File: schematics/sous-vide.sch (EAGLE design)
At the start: 33 parts, among them IC1 MEGA32-P

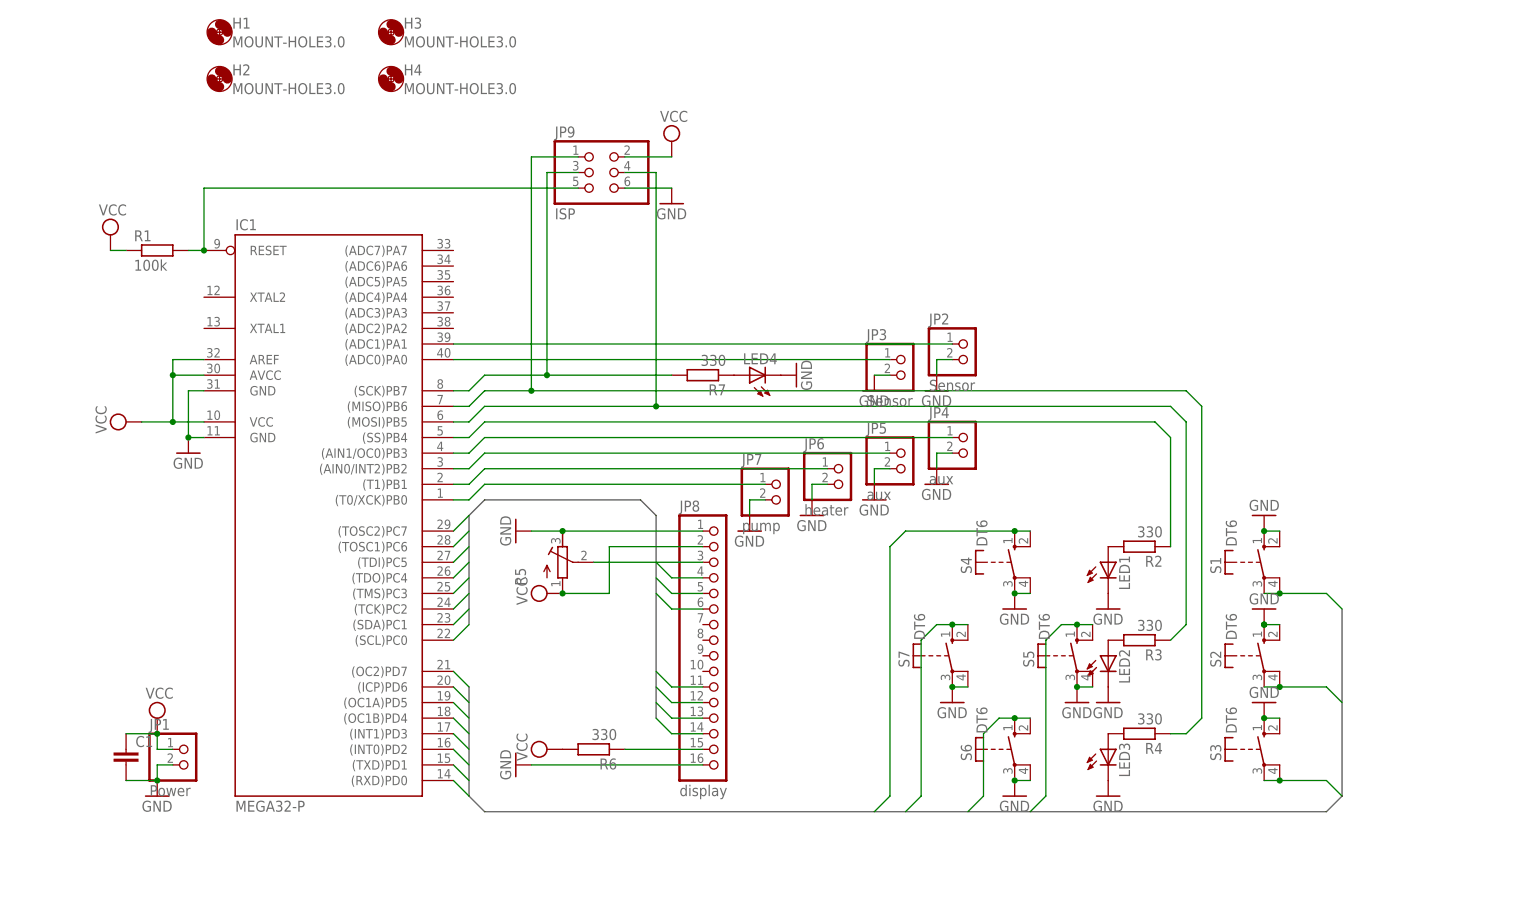
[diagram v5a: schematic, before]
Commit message: Switched to ATmega328 and updated schematics and board.
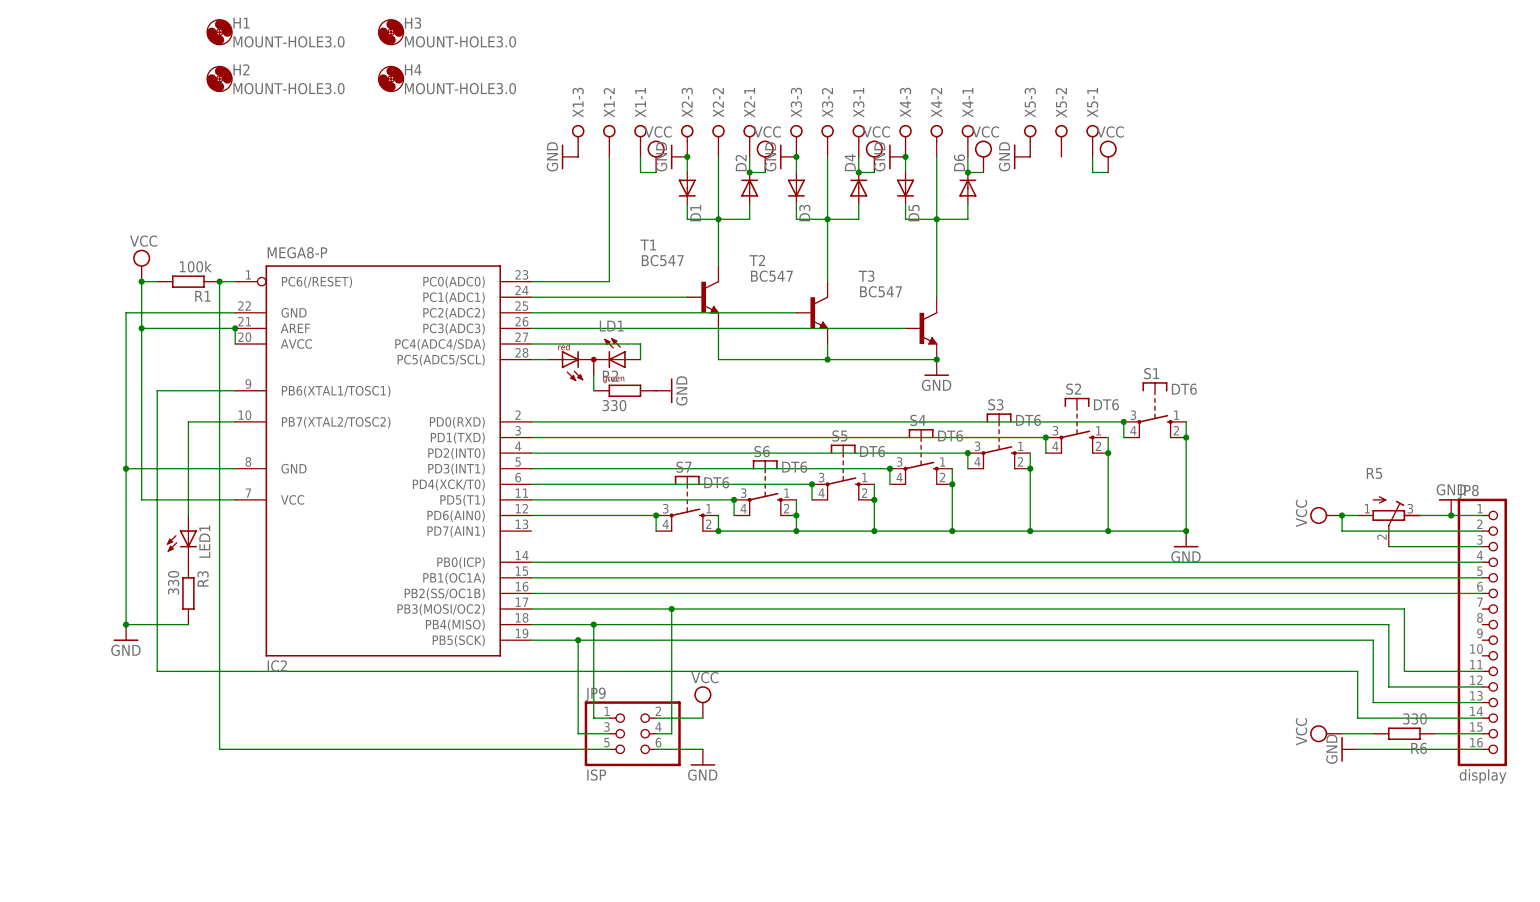
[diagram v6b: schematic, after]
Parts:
- removed C1: (no value), resistor:C-EU025-025X050
- removed IC1: MEGA32-P, atmel:MEGA32-P
- removed JP1: Power, pinhead:PINHD-1X2
- removed JP2, JP3: Sensor, pinhead:PINHD-1X2
- removed JP4, JP5: aux, pinhead:PINHD-1X2
- removed JP6: heater, pinhead:PINHD-1X2
- removed JP7: pump, pinhead:PINHD-1X2
- removed LED2, LED3, LED4: (no value), led:LED3MM
- removed R4, R7: 330, rcl:R-EU_0207/2V
- added D1, D2, D3, D4, D5, D6: (no value), diode:DIODE-D-2.5
- added IC2: MEGA8-P, atmel:MEGA8-P
- added LD1: (no value), led:DUOLED-RG-C
- added T1, T2, T3: BC547, transistor:BC547
- added X1, X2, X3, X4, X5: (no value), con-wago-508:W237-03P
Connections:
- removed net BUTTON0: IC1.(RXD)PD0, S1.P, S1.P@1
- removed net BUTTON1: IC1.(TXD)PD1, S2.P, S2.P@1
- removed net BUTTON2: IC1.(INT0)PD2, S3.P, S3.P@1
- removed net BUTTON3: IC1.(INT1)PD3, S4.S, S4.S@1
- removed net BUTTON4: IC1.(OC1B)PD4, S5.S, S5.S@1
- removed net BUTTON5: IC1.(OC1A)PD5, S6.S, S6.S@1
- removed net BUTTON6: IC1.(ICP)PD6, S7.S, S7.S@1
- removed net BUTTON7: IC1.(OC2)PD7
- removed net DISPLAY0: IC1.(SCL)PC0
- removed net DISPLAY1: IC1.(SDA)PC1, JP8.4
- removed net DISPLAY2: IC1.(TCK)PC2, JP8.5
- removed net DISPLAY3: IC1.(TMS)PC3, JP8.6
- removed net DISPLAY4: IC1.(TDO)PC4, JP8.11
- removed net DISPLAY5: IC1.(TDI)PC5, JP8.12
- removed net DISPLAY6: IC1.(TOSC1)PC6, JP8.13
- removed net DISPLAY7: IC1.(TOSC2)PC7, JP8.14
- removed net N$10: IC1.(SS)PB4, R2.1
- removed net N$11: IC1.(MOSI)PB5, JP9.4, R3.1
- removed net N$12: IC1.(ADC0)PA0, JP3.1
- removed net N$13: IC1.(MISO)PB6, JP9.1, R4.1
- removed net N$16: LED4.A, R7.1
- removed net N$17: IC1.(SCK)PB7, JP9.3, R7.2
- new net N$18: IC2.PB5(SCK), JP8.13, JP9.3
- new net N$19: IC2.PB4(MISO), JP8.12, JP9.1
- new net N$20: IC2.PB0(ICP), JP8.4
- new net N$21: IC2.PB1(OC1A), JP8.5
- new net N$22: IC2.PB2(SS/OC1B), JP8.6
- new net N$23: IC2.PB6(XTAL1/TOSC1), JP8.14
- new net N$24: IC2.PB3(MOSI/OC2), JP8.11, JP9.4
- new net N$26: IC2.PD6(AIN0), S7.P, S7.P@1
- new net N$28: IC2.PD5(T1), S6.P, S6.P@1
- new net N$29: D5.C, D6.A, T3.C, X4-2.KL
- new net N$30: IC2.PD3(INT1), S4.P, S4.P@1
- new net N$31: IC2.PC6(/RESET), JP9.5, R1.1
- new net N$32: IC2.PD4(XCK/T0), S5.P, S5.P@1
- new net N$33: D3.C, D4.A, T2.C, X3-2.KL
- new net N$34: D1.C, D2.A, T1.C, X2-2.KL
- new net N$35: IC2.PD2(INT0), S3.P, S3.P@1
- new net N$36: IC2.PD0(RXD), S1.P, S1.P@1
- new net N$37: IC2.PD1(TXD), S2.P, S2.P@1
- net GND: now also D1.A, D3.A, D5.A, IC2.GND, IC2.GND@1, R2.2, R3.2, S4.S, S4.S@1, S5.S, S5.S@1, S6.S, S6.S@1, S7.S, S7.S@1, T1.E, T2.E, T3.E, X1-3.KL, X2-3.KL, X3-3.KL, X4-3.KL, X5-3.KL; no longer C1.2, IC1.GND, IC1.GND@1, JP1.2, JP2.2, JP3.2, JP4.2, JP5.2, JP6.2, JP7.2, LED1.C, LED2.C, LED3.C, LED4.C, S4.P, S4.P@1, S5.P, S5.P@1, S6.P, S6.P@1, S7.P, S7.P@1
- net N$1: now also LED1.C, R3.1; no longer IC1.(T0/XCK)PB0, JP7.1
- net N$2: now also IC2.PB7(XTAL2/TOSC2), LED1.A; no longer IC1.(T1)PB1, JP6.1
- net N$3: now also IC2.PC0(ADC0), X1-2.KL; no longer IC1.RESET, JP9.5, R1.2
- net N$4: now also IC2.PC1(ADC1), T1.B; no longer IC1.(AIN0/INT2)PB2, JP5.1
- net N$5: now also IC2.PC2(ADC2), T2.B; no longer IC1.(AIN1/OC0)PB3, JP4.1
- net N$6: now also IC2.PC3(ADC3), T3.B; no longer IC1.(ADC1)PA1, JP2.1
- net N$7: now also LD1.C, R2.1; no longer LED3.A, R4.2
- net N$8: now also IC2.PC5(ADC5/SCL), LD1.AR; no longer LED2.A, R3.2
- net N$9: now also IC2.PC4(ADC4/SDA), LD1.AG; no longer LED1.A, R2.2
- net VCC: now also D2.C, D4.C, D6.C, IC2.AREF, IC2.AVCC, IC2.VCC@1, R1.2, X1-1.KL, X2-1.KL, X3-1.KL, X4-1.KL, X5-1.KL; no longer C1.1, IC1.AREF, IC1.AVCC, IC1.VCC, JP1.1, R1.1
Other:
- moved on the sheet: JP8, JP9, LED1, R1, R2, R3, R5, R6, S1, S2, S3, S4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

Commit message: Changed connectors and renumbered parts on schematic and board.
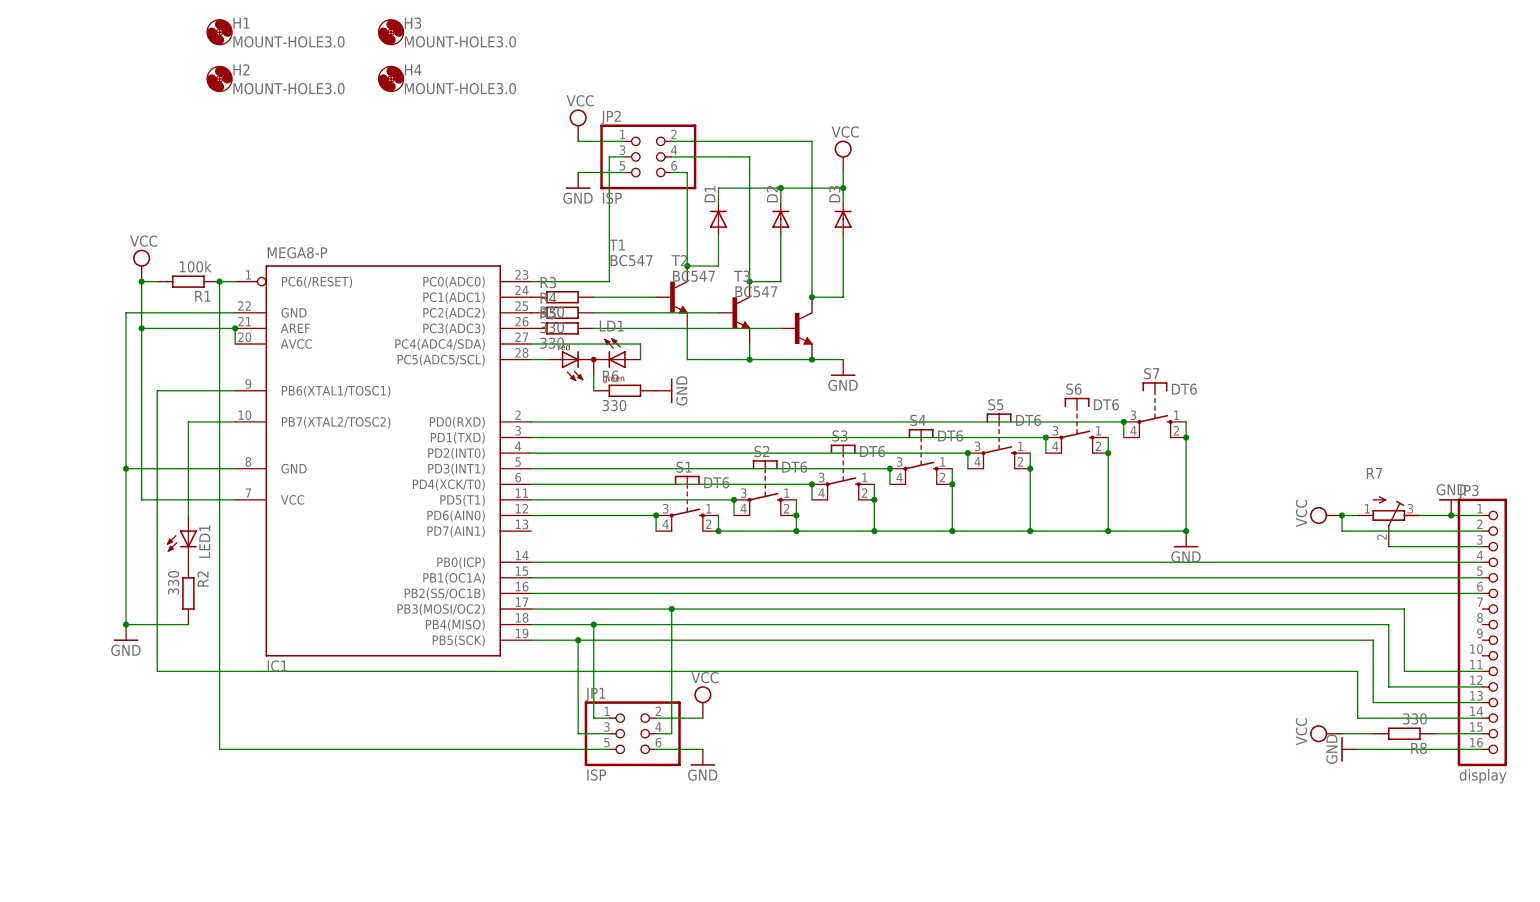
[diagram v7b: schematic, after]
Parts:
- removed D4, D5, D6: (no value), diode:DIODE-D-2.5
- removed X1, X2, X3, X4, X5: (no value), con-wago-508:W237-03P
- added JP2: ISP, pinhead:PINHD-2X3
- added R4, R8: 330, rcl:R-EU_0207/2V
- added R7: (no value), resistor:R-TRIMM3339P
- R5: value (none) -> 330; device resistor:R-TRIMM3339P -> rcl:R-EU_0207/2V
- renumbered IC2 to IC1, JP8 to JP3, JP9 to JP1
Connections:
- removed net N$29: D5.C, D6.A, T3.C, X4-2.KL
- removed net N$33: D3.C, D4.A, T2.C, X3-2.KL
- removed net N$34: D1.C, D2.A, T1.C, X2-2.KL
- new net N$10: R3.2, T1.B
- new net N$11: R4.2, T2.B
- new net N$12: R5.2, T3.B
- new net N$13: D1.A, JP2.6, T1.C
- new net N$16: D2.A, JP2.4, T2.C
- new net N$17: D3.A, JP2.2, T3.C
- net GND: now also JP2.5, R6.2, R7.A; no longer D1.A, D3.A, D5.A, R3.2, R5.A, X1-3.KL, X2-3.KL, X3-3.KL, X4-3.KL, X5-3.KL
- net N$1: now also R2.1; no longer R3.1
- net N$14: now also R7.S; no longer R5.S
- net N$15: now also R8.1; no longer R6.1
- net N$26: now also S1.P, S1.P@1; no longer S7.P, S7.P@1
- net N$28: now also S2.P, S2.P@1; no longer S6.P, S6.P@1
- net N$3: now also JP2.3; no longer X1-2.KL
- net N$32: now also S3.P, S3.P@1; no longer S5.P, S5.P@1
- net N$35: now also S5.P, S5.P@1; no longer S3.P, S3.P@1
- net N$36: now also S7.P, S7.P@1; no longer S1.P, S1.P@1
- net N$37: now also S6.P, S6.P@1; no longer S2.P, S2.P@1
- net N$4: now also R3.1; no longer T1.B
- net N$5: now also R4.1; no longer T2.B
- net N$6: now also R5.1; no longer T3.B
- net N$7: now also R6.1; no longer R2.1
- net VCC: now also D1.C, D3.C, JP2.1, R7.E, R8.2; no longer D4.C, D6.C, R5.E, R6.2, X1-1.KL, X2-1.KL, X3-1.KL, X4-1.KL, X5-1.KL
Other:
- moved on the sheet: D1, D2, D3, R2, R3, R6, S1, S2, S3, S5, S6, S7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

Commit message: minor tweaks in component placement, sent to pcb manufacturer
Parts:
- JP2: value ISP -> IO
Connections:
- net N$31: now also R1.2; no longer R1.1
- net VCC: now also R1.1; no longer R1.2
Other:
- moved on the sheet: R1
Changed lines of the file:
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@@
 <part name="R4" library="rcl" deviceset="R-EU_" device="0207/2V" value="330"/>
 <part name="R5" library="rcl" deviceset="R-EU_" device="0207/2V" value="330"/>
-<part name="JP2" library="pinhead" deviceset="PINHD-2X3" device="" value="ISP"/>
+<part name="JP2" library="pinhead" deviceset="PINHD-2X3" device="" value="IO"/>
 </parts>
 <sheets>
@@
 <instances>
 <instance part="SUPPLY1" gate="G$1" x="7.62" y="93.98"/>
-<instance part="R1" gate="G$1" x="15.24" y="91.44" rot="R180"/>
+<instance part="R1" gate="G$1" x="15.24" y="91.44"/>
 <instance part="JP3" gate="A" x="228.6" y="35.56"/>
 <instance part="S7" gate="1" x="172.72" y="68.58" rot="R270"/>
@@
 <junction x="22.86" y="83.82"/>
 <wire x1="22.86" y1="83.82" x2="7.62" y2="83.82" width="0.1524" layer="91"/>
-<pinref part="R1" gate="G$1" pin="2"/>
-<wire x1="10.16" y1="91.44" x2="7.62" y2="91.44" width="0.1524" layer="91"/>
+<junction x="7.62" y="83.82"/>
+<pinref part="R1" gate="G$1" pin="1"/>
+<wire x1="7.62" y1="91.44" x2="10.16" y2="91.44" width="0.1524" layer="91"/>
 <junction x="7.62" y="91.44"/>
-<junction x="7.62" y="83.82"/>
 </segment>
 <segment>
@@
 <pinref part="JP1" gate="A" pin="5"/>
 <wire x1="20.32" y1="15.24" x2="83.82" y2="15.24" width="0.1524" layer="91"/>
+<pinref part="R1" gate="G$1" pin="2"/>
+<wire x1="20.32" y1="15.24" x2="20.32" y2="91.44" width="0.1524" layer="91"/>
 <pinref part="IC1" gate="G$1" pin="PC6(/RESET)"/>
-<pinref part="R1" gate="G$1" pin="1"/>
-<wire x1="22.86" y1="91.44" x2="20.32" y2="91.44" width="0.1524" layer="91"/>
-<wire x1="20.32" y1="91.44" x2="20.32" y2="15.24" width="0.1524" layer="91"/>
+<wire x1="20.32" y1="91.44" x2="22.86" y2="91.44" width="0.1524" layer="91"/>
 <junction x="20.32" y="91.44"/>
 </segment>
